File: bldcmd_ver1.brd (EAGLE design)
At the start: 43 x 49 mm, 94 parts, among them CN1 DF61-2P-2.2V(23), IC1 STSPIN32F0, IC2 AS5047P-ATSM, IC3 ADM4852ACPZ-REEL7, J1 DF65-3P-1.7V(21), Q1 PSMN2R4-30MLD, Q2 PSMN2R4-30MLD, Q3 PSMN2R4-30MLD, Q4 PSMN2R4-30MLD, Q5 PSMN2R4-30MLD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

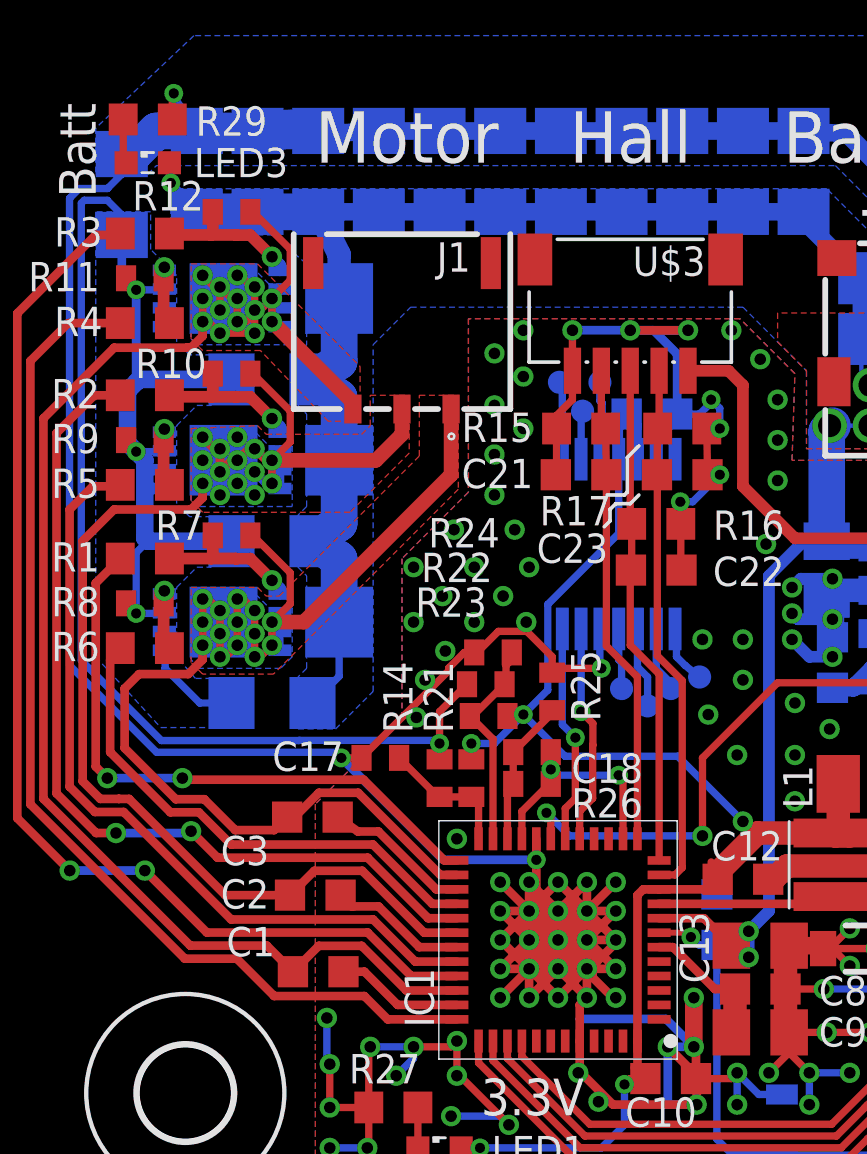
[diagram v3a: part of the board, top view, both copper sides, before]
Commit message: #2 の対応，MCUをstspin32F0Aに変更
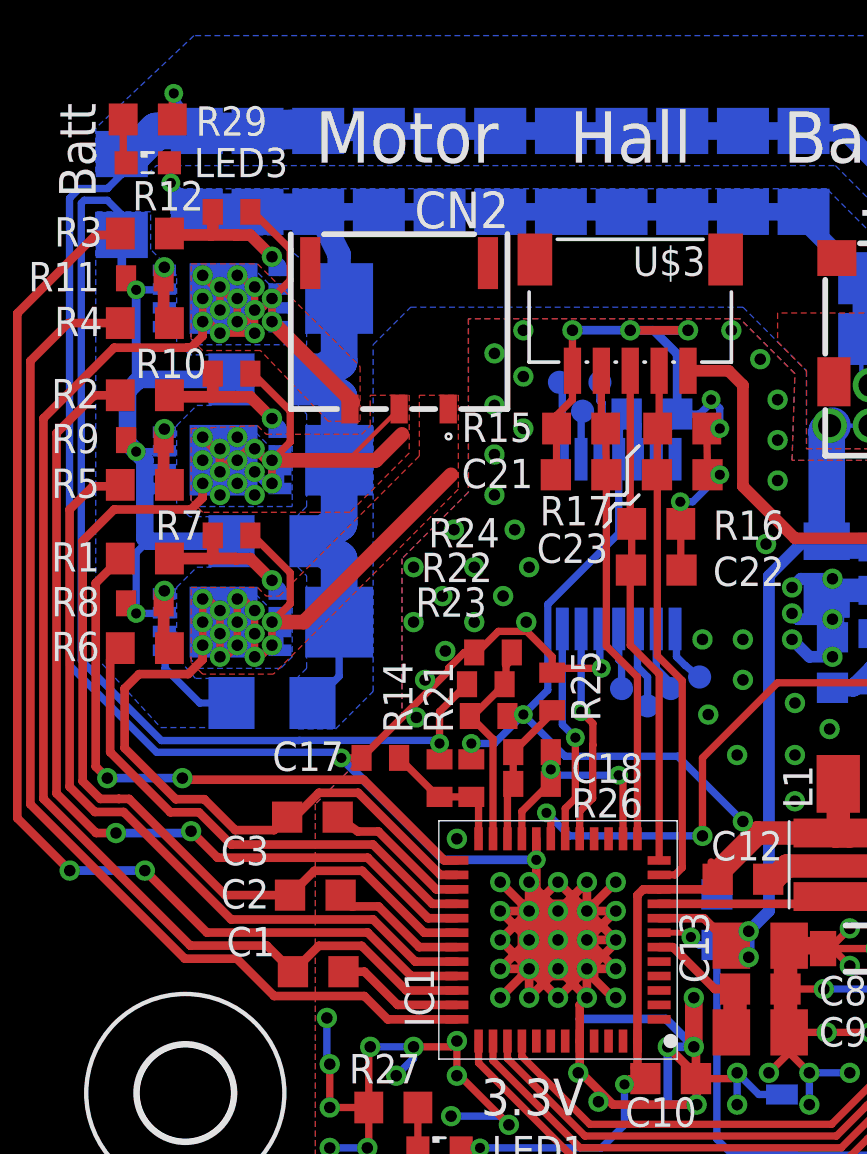
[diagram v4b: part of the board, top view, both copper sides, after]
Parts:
- removed J1: DF65-3P-1.7V(21), scramble-con-hirose:DF65-3P-1.7V
- added CN2: DF65-3P-1.7V(21), scramble-con-hirose:DF65-3P-1.7V
- IC1: value STSPIN32F0 -> STSPIN32F0A; device rcssl_lib:QFN50P700X700X100-49N -> scramble-mcu:VFQFPN48_7X7X1.0-48L
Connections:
- net MOT_U: now also CN2.3; no longer J1.3
- net MOT_V: now also CN2.2; no longer J1.2
- net MOT_W: now also CN2.1; no longer J1.1
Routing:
- net MOT_V: track 56.3 -> 60.4 mm
- net MOT_W: track 46.6 -> 44.3 mm
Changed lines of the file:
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@@
 <?xml version="1.0" encoding="utf-8"?>
 <!DOCTYPE eagle SYSTEM "eagle.dtd">
-<eagle version="8.3.2">
+<eagle version="8.4.0">
 <drawing>
 <settings>
@@
 <param name="dpMaxLengthDifference" value="10mm"/>
 <param name="dpGapFactor" value="2.5"/>
-<param name="checkGrid" value="0"/>
-<param name="checkAngle" value="0"/>
 <param name="checkFont" value="1"/>
 <param name="checkRestrict" value="0"/>
+<param name="checkStop" value="0"/>
 <param name="useDiameter" value="13"/>
 <param name="maxErrors" value="50"/>
@@
 <attribute name="VALUE" x="11.7" y="14.2" size="1.016" layer="27" rot="R180"/>
 </element>
-<element name="IC1" library="rcssl_lib" package="QFN50P700X700X100-49N" value="STSPIN32F0" x="19.4" y="8.3" smashed="yes" rot="R180">
+<element name="IC1" library="scramble-mcu" package="VFQFPN48_7X7X1.0-48L" value="STSPIN32F0A" x="19.4" y="8.3" smashed="yes" rot="R180">
 <attribute name="3D_PACKAGE" value="" x="19.4" y="8.3" size="1.778" layer="27" rot="R180" display="off"/>
 <attribute name="ALLIED_NUMBER" value="" x="19.4" y="8.3" size="1.778" layer="27" rot="R180" display="off"/>
-<attribute name="DESCRIPTION" value="Motor / Motion / Ignition Controllers &amp; Drivers Advance BLDC Contrlr w/Embedded STM32 MCU" x="19.4" y="8.3" size="1.778" layer="27" rot="R180" display="off"/>
+<attribute name="DESCRIPTION" value="Advanced BLDC controller with embedded STM32 MCU" x="19.4" y="8.3" size="1.778" layer="27" rot="R180" display="off"/>
 <attribute name="HEIGHT" value="1mm" x="19.4" y="8.3" size="1.778" layer="27" rot="R180" display="off"/>
 <attribute name="MANUFACTURER_NAME" value="STMicroelectronics" x="19.4" y="8.3" size="1.778" layer="27" rot="R180" display="off"/>
-<attribute name="MANUFACTURER_PART_NUMBER" value="STSPIN32F0" x="19.4" y="8.3" size="1.778" layer="27" rot="R180" display="off"/>
+<attribute name="MANUFACTURER_PART_NUMBER" value="STSPIN32F0ATR" x="19.4" y="8.3" size="1.778" layer="27" rot="R180" display="off"/>
 <attribute name="NAME" x="14.6" y="6.3" size="1.016" layer="25" rot="R270" align="center"/>
 <attribute name="OTHER_PART_NUMBER" value="" x="19.4" y="8.3" size="1.778" layer="27" rot="R180" display="off"/>
@@
 <attribute name="NAME" x="32.9" y="12.4" size="1.016" layer="25"/>
 <attribute name="VALUE" x="29" y="11.6" size="1.016" layer="27"/>
-</element>
-<element name="J1" library="scramble-con-hirose" package="DF65-3P-1.7V" value="DF65-3P-1.7V(21)" x="14" y="29.7" smashed="yes" rot="R180">
-<attribute name="3D_PACKAGE" value="" x="14" y="29.7" size="1.778" layer="27" rot="R180" display="off"/>
-<attribute name="ALLIED_NUMBER" value="" x="14" y="29.7" size="1.778" layer="27" rot="R180" display="off"/>
-<attribute name="DESCRIPTION" value="Hirose DF Series, Series Number 65, 1.7mm Pitch 3 Way 1 Row Straight PCB Header, Solder Termination, 4A" x="14" y="29.7" size="1.778" layer="27" rot="R180" display="off"/>
-<attribute name="HEIGHT" value="mm" x="14" y="29.7" size="1.778" layer="27" rot="R180" display="off"/>
-<attribute name="MANUFACTURER_NAME" value="Hirose" x="14" y="29.7" size="1.778" layer="27" rot="R180" display="off"/>
-<attribute name="MANUFACTURER_PART_NUMBER" value="DF65-3P-1.7V(21)" x="14" y="29.7" size="1.778" layer="27" rot="R180" display="off"/>
-<attribute name="NAME" x="15.789" y="31.937" size="1.016" layer="25" align="center"/>
-<attribute name="OTHER_PART_NUMBER" value="" x="14" y="29.7" size="1.778" layer="27" rot="R180" display="off"/>
-<attribute name="RS_PART_NUMBER" value="8735164" x="14" y="29.7" size="1.778" layer="27" rot="R180" display="off"/>
-<attribute name="SUPPLIER_NAME" value="RS" x="14" y="29.7" size="1.778" layer="27" rot="R180" display="off"/>
 </element>
 <element name="D1" library="diode" library_urn="urn:adsk.eagle:library:210" package="SOD123FL" package3d_urn="urn:adsk.eagle:package:43458/1" value="SMF5.0AT1" x="30.2" y="8" smashed="yes" rot="R180">
@@
 <attribute name="SUPPLIER_NAME" value="RS" x="31.2" y="29.3" size="1.778" layer="27" rot="R180" display="off"/>
 <attribute name="VALUE" x="33.8" y="33.9" size="1.27" layer="27" font="vector" ratio="12" rot="R180"/>
+</element>
+<element name="CN2" library="scramble-con-hirose" package="DF65-3P-1.7V" value="DF65-3P-1.7V(21)" x="13.9" y="29.7" rot="R180">
+<attribute name="3D_PACKAGE" value="" x="13.9" y="29.7" size="1.778" layer="27" rot="R180" display="off"/>
+<attribute name="ALLIED_NUMBER" value="" x="13.9" y="29.7" size="1.778" layer="27" rot="R180" display="off"/>
+<attribute name="DESCRIPTION" value="Hirose DF Series, Series Number 65, 1.7mm Pitch 3 Way 1 Row Straight PCB Header, Solder Termination, 4A" x="13.9" y="29.7" size="1.778" layer="27" rot="R180" display="off"/>
+<attribute name="HEIGHT" value="mm" x="13.9" y="29.7" size="1.778" layer="27" rot="R180" display="off"/>
+<attribute name="MANUFACTURER_NAME" value="Hirose" x="13.9" y="29.7" size="1.778" layer="27" rot="R180" display="off"/>
+<attribute name="MANUFACTURER_PART_NUMBER" value="DF65-3P-1.7V(21)" x="13.9" y="29.7" size="1.778" layer="27" rot="R180" display="off"/>
+<attribute name="OTHER_PART_NUMBER" value="" x="13.9" y="29.7" size="1.778" layer="27" rot="R180" display="off"/>
+<attribute name="RS_PART_NUMBER" value="8735164" x="13.9" y="29.7" size="1.778" layer="27" rot="R180" display="off"/>
+<attribute name="SUPPLIER_NAME" value="RS" x="13.9" y="29.7" size="1.778" layer="27" rot="R180" display="off"/>
 </element>
 </elements>
@@
 <via x="9.5" y="30.5" extent="1-16" drill="0.4"/>
 <via x="9.5" y="29.7" extent="1-16" drill="0.4"/>
-<contactref element="J1" pad="3"/>
 <wire x1="7.1" y1="29.7" x2="7.1" y2="29.2" width="0.3" layer="1"/>
 <wire x1="9.5" y1="30.5" x2="10.1318" y2="31.1318" width="0.254" layer="1"/>
@@
 <wire x1="9.3222" y1="8.1028" x2="6.67116875" y2="8.1028" width="0.3" layer="1"/>
 <wire x1="6.67116875" y1="8.1028" x2="1.5904" y2="13.18356875" width="0.3" layer="1"/>
-<wire x1="12.3" y1="26.675" x2="12.3" y2="26.9" width="0.508" layer="1"/>
 <wire x1="12.3" y1="26.9" x2="9.5" y2="29.7" width="0.508" layer="1"/>
 <wire x1="7.1" y1="29.7" x2="7.3" y2="29.7" width="0.254" layer="1"/>
@@
 <wire x1="15.9" y1="6.55" x2="14.15" y2="6.55" width="0.3" layer="1"/>
 <wire x1="14.15" y1="6.55" x2="12.6048" y2="8.0952" width="0.3" layer="1"/>
+<contactref element="CN2" pad="3"/>
 </signal>
 <signal name="MOT_V">
@@
 <contactref element="IC1" pad="30"/>
 <contactref element="C2" pad="2"/>
-<contactref element="J1" pad="2"/>
 <polygon width="0.1524" layer="16" thermals="no">
 <vertex x="10.2" y="23.3"/>
@@
 <wire x1="8.8723" y1="27.7777" x2="8.96100625" y2="27.7777" width="0.254" layer="1"/>
 <wire x1="8.96100625" y1="27.7777" x2="10.1318" y2="26.60690625" width="0.254" layer="1"/>
-<wire x1="10.1318" y1="25.5318" x2="9.5" y2="24.9" width="0.254" layer="1"/>
+<wire x1="9.6" y1="25" x2="10.1318" y2="25.5318" width="0.254" layer="1"/>
+<wire x1="9.6" y1="25" x2="9.5" y2="24.9" width="0.254" layer="1"/>
 <wire x1="10.1318" y1="26.60690625" x2="10.1318" y2="25.5318" width="0.254" layer="1"/>
 <wire x1="10.125" y1="9.85" x2="9.875" y2="9.5" width="0.3" layer="1"/>
@@
 <wire x1="7.88499375" y1="9.85" x2="4.55489375" y2="13.1801" width="0.3" layer="1"/>
 <wire x1="10.125" y1="9.85" x2="7.88499375" y2="9.85" width="0.3" layer="1"/>
-<wire x1="14" y1="26.675" x2="14" y2="25.8" width="0.508" layer="1"/>
 <wire x1="14" y1="25.8" x2="13.1" y2="24.9" width="0.508" layer="1"/>
 <wire x1="13.1" y1="24.9" x2="9.5" y2="24.9" width="0.508" layer="1"/>
@@
 <wire x1="12.62525625" y1="10.6924" x2="10.9674" y2="10.6924" width="0.3" layer="1"/>
 <wire x1="10.9674" y1="10.6924" x2="10.125" y2="9.85" width="0.3" layer="1"/>
+<contactref element="CN2" pad="2"/>
+<wire x1="13.9" y1="26.675" x2="12.225" y2="25" width="0.1524" layer="1"/>
+<wire x1="12.225" y1="25" x2="9.6" y2="25" width="0.1524" layer="1"/>
 </signal>
 <signal name="MOT_W">
@@
 <via x="9.5" y="19.3" extent="1-16" drill="0.4"/>
 <via x="9.5" y="18.5" extent="1-16" drill="0.4"/>
-<contactref element="J1" pad="1"/>
 <wire x1="7.1" y1="18" x2="7.1" y2="18.5" width="0.3" layer="1"/>
 <wire x1="7.1" y1="18" x2="6.6" y2="17.5" width="0.3" layer="1"/>
@@
 <wire x1="6.169896875" y1="13.169896875" x2="7.158621875" y2="13.169896875" width="0.3" layer="1"/>
 <wire x1="7.158621875" y1="13.169896875" x2="8.22851875" y2="12.1" width="0.3" layer="1"/>
-<wire x1="15.7" y1="26.675" x2="15.7" y2="24.4" width="0.508" layer="1"/>
 <wire x1="15.7" y1="24.4" x2="10.6" y2="19.3" width="0.508" layer="1"/>
 <wire x1="10.6" y1="19.3" x2="9.6" y2="19.3" width="0.508" layer="1"/>
@@
 <wire x1="15.9" y1="10.55" x2="15.32683125" y2="10.55" width="0.3" layer="1"/>
 <wire x1="15.32683125" y1="10.55" x2="12.48443125" y2="13.3924" width="0.3" layer="1"/>
+<contactref element="CN2" pad="1"/>
 </signal>
 <signal name="N$9">

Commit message: #3 の対応，エンコーダ入力からSPI接続に変更
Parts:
- removed TP4, TP5, TP6, TP7: TPTP08R, testpad:TP08R
- moved C19 2.00 mm to (28.9, 19.9)
- moved C20 2.00 mm to (28.7, 23.1)
- moved U$6 2.00 mm to (32.3, 22.4)
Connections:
- net N$10 renamed OC_COMP
- removed net ENC_A: IC1.18, IC2.7
- removed net ENC_B: IC1.17, IC2.6
- net N$12: now also IC1.17; no longer TP6.TP
- net N$17: now also IC1.18; no longer TP7.TP
- net N$7: now also IC1.15; no longer TP4.TP
- net N$8: now also IC1.16; no longer TP5.TP
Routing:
- net ENC_B: track 7.62 -> 0.00 mm, vias 1 -> 0
- net ENC_A: track 7.59 -> 0.00 mm, vias 1 -> 0
- net +5V: track 40.4 -> 33.0 mm, vias 1 -> 2
- net N$17: track 2.10 -> 8.36 mm, vias 0 -> 1
- net N$7: track 2.05 -> 8.21 mm, vias 0 -> 1
- net N$8: track 2.27 -> 8.15 mm, vias 0 -> 1
- net N$12: track 2.81 -> 8.09 mm, vias 0 -> 1
- net GND: track 306.8 -> 303.8 mm, vias 156 -> 150
- net N$23: track 16.7 -> 17.3 mm

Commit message: 修正したSHコネクタの変更を適用
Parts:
- removed U$2, U$3: SM05B-SRSS-TB, JST-SH:SM05B-SRSS-TB
- removed U$4, U$5: SM04B-SRSS-TB, JST-SH:SM04B-SRSS-TB
- added CN3, CN4: SM04B-SRSS-TB, scramble-con-jst:SM04B-SRSS-TB
- added CN5, CN6: SM05B-SRSS-TB, scramble-con-jst:SM05B-SRSS-TB
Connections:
- net +3V3: now also CN6.5; no longer U$2.5
- net +5V: now also CN4.3, CN5.5; no longer U$3.5, U$5.3
- net GND: now also CN3.4, CN4.4, CN5.1, CN6.3; no longer U$2.3, U$3.1, U$4.4, U$5.4
- net N$23: now also CN5.2; no longer U$3.2
- net N$24: now also CN5.3; no longer U$3.3
- net N$25: now also CN5.4; no longer U$3.4
- net N$29: now also CN3.2; no longer U$4.2
- net N$30: now also CN3.3; no longer U$4.3
- net N$32: now also CN3.1; no longer U$4.1
- net NRST: now also CN6.1; no longer U$2.1
- net SWCLK: now also CN6.4; no longer U$2.4
- net SWDIO: now also CN6.2; no longer U$2.2
- net UART_RX: now also CN4.2; no longer U$5.2
- net UART_TX: now also CN4.1; no longer U$5.1
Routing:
- net GND: track 303.8 -> 293.0 mm
- net +3V3: track 62.1 -> 56.0 mm
- net N$24: track 17.7 -> 12.5 mm
- net +5V: track 33.0 -> 29.6 mm
- net NRST: track 27.3 -> 24.9 mm
- net N$25: track 18.5 -> 16.5 mm
- net N$23: track 17.3 -> 15.5 mm
- net N$30: track 4.62 -> 3.22 mm
- net N$32: track 2.82 -> 1.62 mm
- net N$29: track 2.61 -> 1.41 mm
- net SWDIO: track 30.1 -> 28.9 mm
- net SWCLK: track 30.5 -> 29.4 mm
- net UART_RX: track 37.1 -> 36.1 mm
- net UART_TX: track 38.8 -> 37.8 mm

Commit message: ST-Linkのコネクタの接続順を入れ替えた
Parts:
- moved CN6 72.4 mm to (40.2, 10.5), flipped to the bottom, turned to 270 degrees
- moved CN5 66.4 mm to (22.8, 45.2), turned to 180 degrees
- moved CN4 11.5 mm to (48.5, 18.9)
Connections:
- net +3V3: now also CN6.1; no longer CN6.5
- net NRST: now also CN6.5; no longer CN6.1
- net SWCLK: now also CN6.2; no longer CN6.4
- net SWDIO: now also CN6.4; no longer CN6.2
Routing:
- net +3V3: track 56.0 -> 62.3 mm
- net NRST: track 24.9 -> 27.7 mm
- net SWDIO: track 28.9 -> 30.1 mm
- net SWCLK: track 29.4 -> 30.3 mm

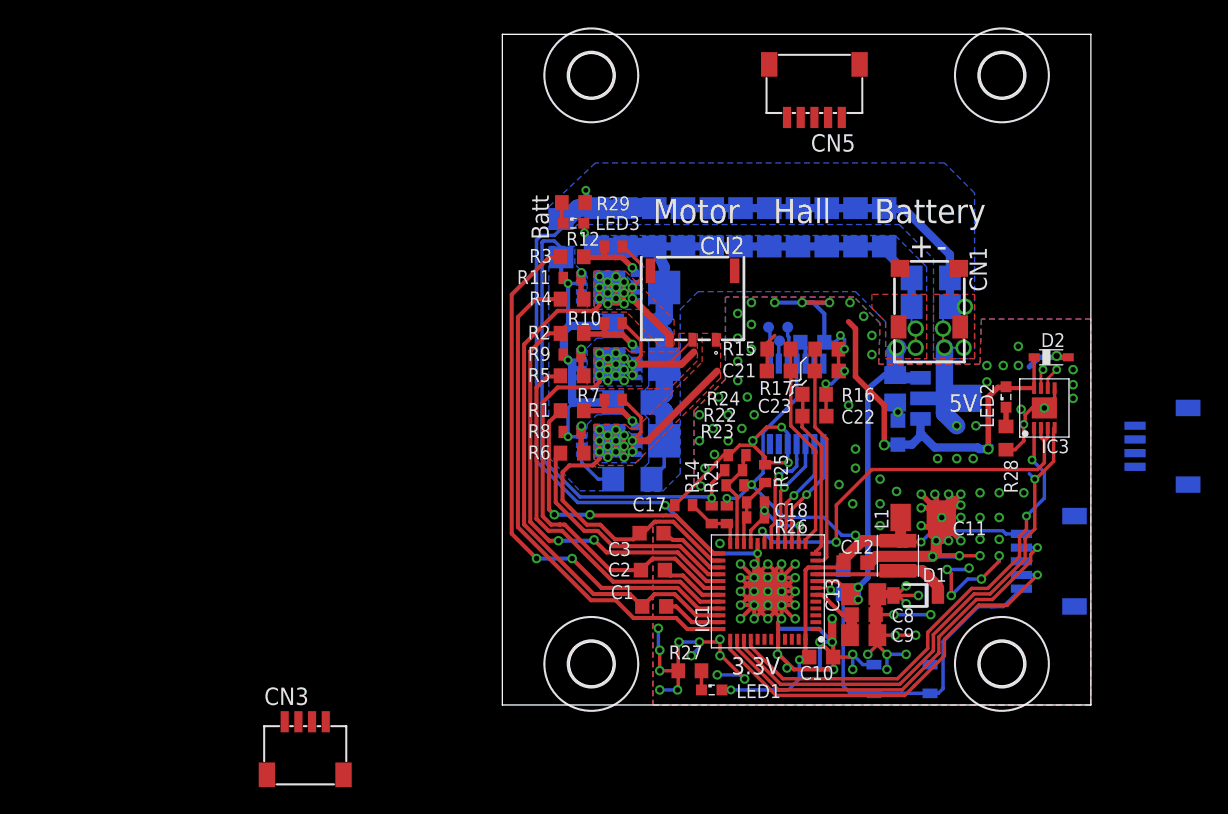
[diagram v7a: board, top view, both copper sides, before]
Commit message: 3端子レギュレータのライブラリ変更の反映 SHコネクタの接続順を反転
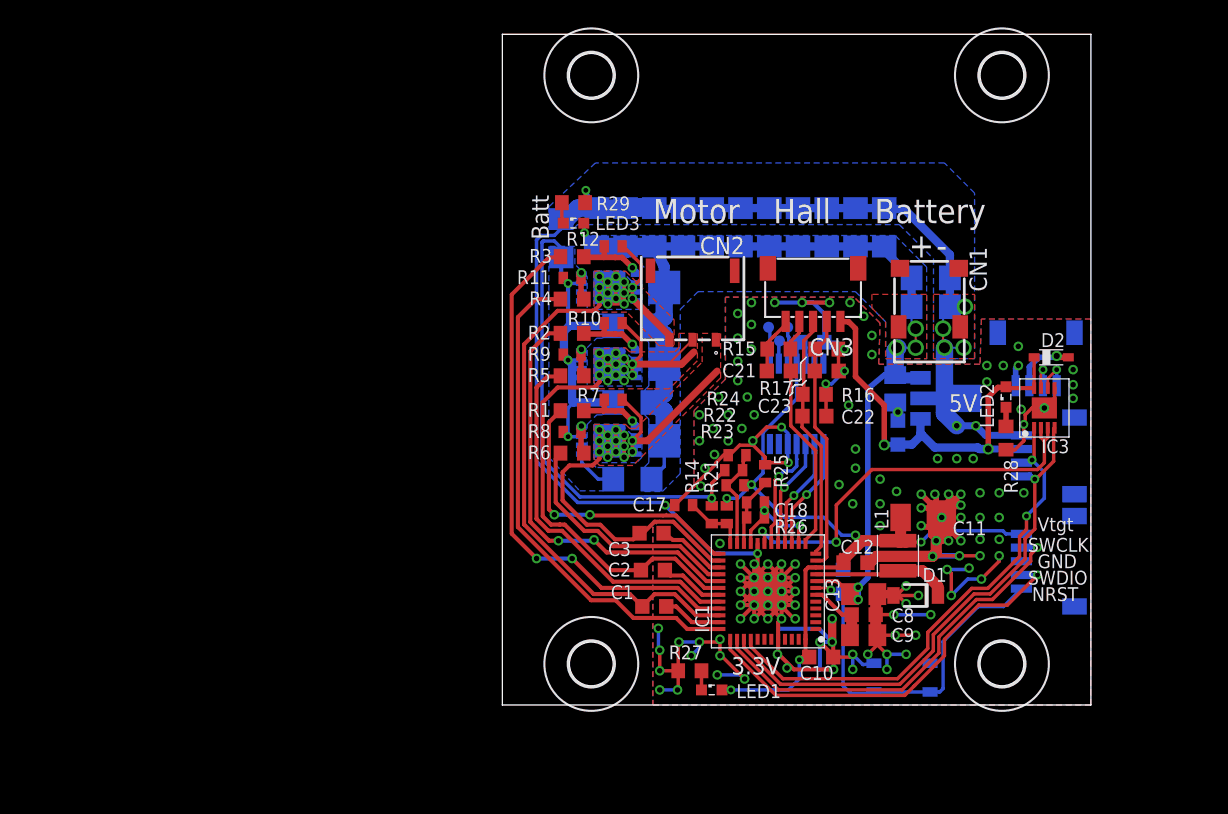
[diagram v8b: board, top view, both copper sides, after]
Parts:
- removed CN5: SM05B-SRSS-TB, scramble-con-jst:SM05B-SRSS-TB
- added CN7: SM04B-SRSS-TB, scramble-con-jst:SM04B-SRSS-TB
- C21, C22, C23: value (none) -> 10p
- CN3: value SM04B-SRSS-TB -> SM05B-SRSS-TB; device scramble-con-jst:SM04B-SRSS-TB -> scramble-con-jst:SM05B-SRSS-TB
- U$6: value NJM78L05A -> NJM78L05S; device rcssl_lib:SOT89R -> scramble-mcu:SOT89R
- moved CN3 50.2 mm to (22.7, 30.3), turned to 180 degrees
- moved CN4 8.33 mm to (40.2, 18.2)
- moved SW1 0.10 mm to (29.2, 2.00)
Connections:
- net +5V: now also CN3.1, CN4.2; no longer CN4.3, CN5.5
- net GND: now also CN3.5, CN4.1, CN7.1; no longer CN3.4, CN4.4, CN5.1
- net N$23: now also CN3.4; no longer CN5.2
- net N$24: now also CN3.3; no longer CN5.3
- net N$25: now also CN3.2; no longer CN5.4
- net N$29: now also CN7.3; no longer CN3.2
- net N$30: now also CN7.2; no longer CN3.3
- net N$32: now also CN7.4; no longer CN3.1
- net UART_RX: now also CN4.3; no longer CN4.2
- net UART_TX: now also CN4.4; no longer CN4.1
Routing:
- net GND: track 293.0 -> 300.1 mm, vias 150 -> 149
- net N$24: track 12.5 -> 18.1 mm
- net +5V: track 29.6 -> 32.4 mm
- net N$25: track 16.5 -> 19.0 mm
- net N$23: track 15.5 -> 17.8 mm
- net N$30: track 3.22 -> 4.60 mm
- net N$32: track 1.62 -> 2.79 mm
- net N$29: track 1.41 -> 2.59 mm
- net UART_TX: track 37.8 -> 38.9 mm
- net UART_RX: track 36.1 -> 37.0 mm
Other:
- board text added: "GND"
- board text added: "NRST"
- board text added: "SWCLK"
- board text added: "SWDIO"
- board text added: "Vtgt"
